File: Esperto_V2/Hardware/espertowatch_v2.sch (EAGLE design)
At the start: 50 parts, among them J1 SM02B, J2 47346-0001, Q1 DMP2035U, U1 AP2112K-3.3V, U2 MCP73832, U3 MAX1921EUT18+T, U4 ATSAMD21G-A, U5 MAX30102EFD+, U6 MAX14595ETAT, U7 MB85RC256VPF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

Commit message: Added new hardware and EAGLE libraries
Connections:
- net 3V3: now also J3.7; no longer J3.2
- net GND: now also J3.4, J3.8; no longer J3.1, J3.5
- net SCL: now also J3.6; no longer J3.3
- net SDA: now also J3.5; no longer J3.4
- net SWCLK: now also J3.2; no longer J3.7
- net SWDIO: now also J3.1; no longer J3.8
- net SWRST: now also J3.3; no longer J3.6
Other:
- moved on the sheet: J3

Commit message: BLE support for APP - bug fixes
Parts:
- C15, C18: value 1uF -> 1.0uF; device CAPACITOR:C-EUC0402_MURATA_GRM15-GJM15 -> CAPACITOR:C-EUC0603_MURATA_GRM18
- C21, C3: device CAPACITOR:C-EUC0201_MURATA_GRM03 -> CAPACITOR:C-EUC0402_MURATA_GRM15-GJM15
- C4, C9: device CAPACITOR:C-EUC0402_MURATA_GRM15-GJM15 -> CAPACITOR:C-EUC0603_MURATA_GRM18
- L1: device INDUCTOR:L-EUL0402_MURATA_LQP15_LQG15 -> INDUCTOR:L-EUL0805_TDK_MLZ
- R1, R4: device RESISTOR:CRCW02011M00FKED -> RESISTOR:CRCW04021M00FKED
- R12, R5: device RESISTOR:CRCW0402100KFKED -> RESISTOR:R-EU_R0603_VISHAY_MCT0603
- R2: device RESISTOR:CRCW0201100KFKED -> RESISTOR:R-EU_R0603_VISHAY_MCT0603
- R7: device RESISTOR:CRCW040210K0FKED -> RESISTOR:R-EU_R0402_VISHAY_CRCW0402
- U3: value MAX1921EUT18+T -> MAX1921EUT18+
- U6: value MAX14595ETAT -> MAX14595ETA+
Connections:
- net GND: now also R5.1; no longer R5.2
- net VUSB: now also R5.2; no longer R5.1
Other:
- moved on the sheet: R5

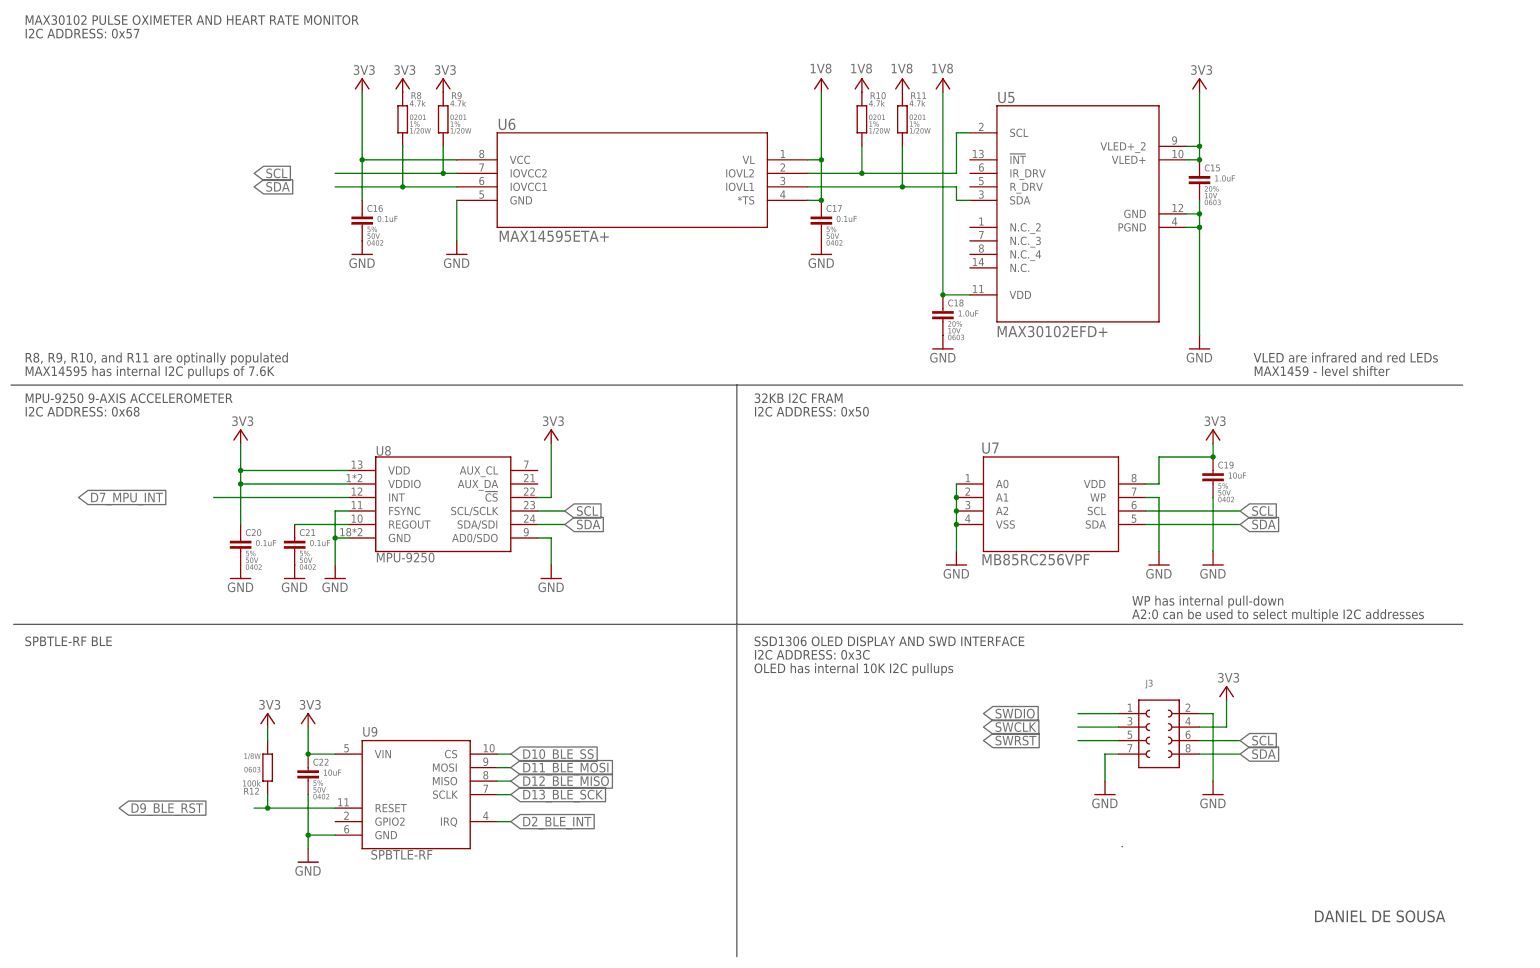
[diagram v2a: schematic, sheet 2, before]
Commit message: Removed I2C pullups
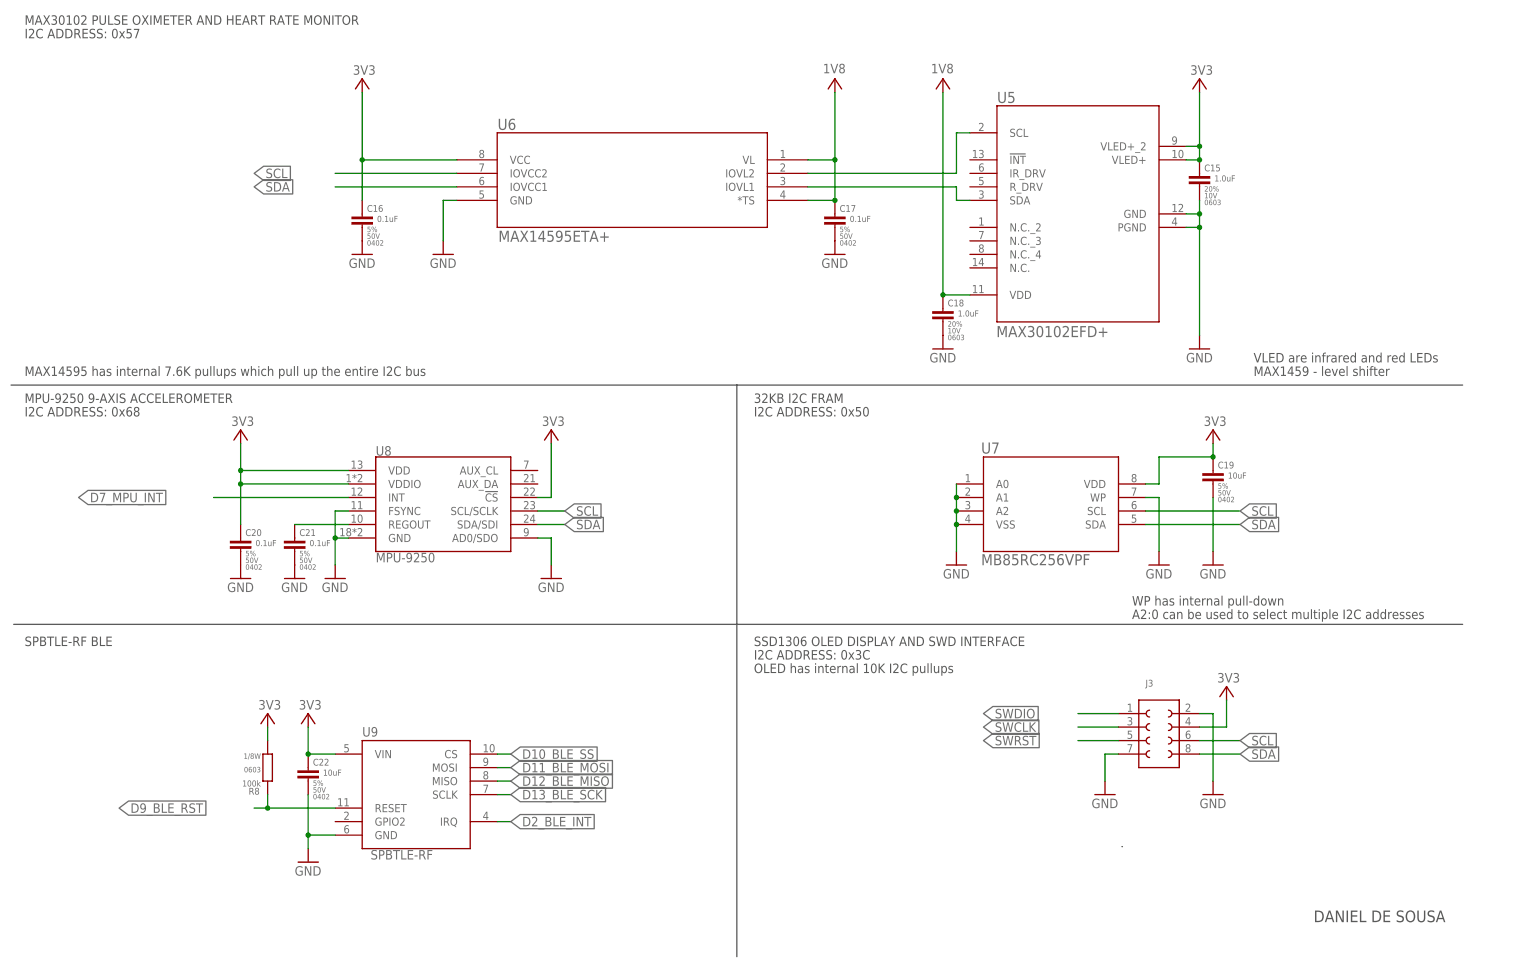
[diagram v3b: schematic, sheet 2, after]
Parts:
- removed R10, R11, R9: 4.7k, RESISTOR:CRCW02014K70FKED
- removed R12: 100k, RESISTOR:R-EU_R0603_VISHAY_MCT0603
- R8: value 4.7k -> 100k; device RESISTOR:CRCW02014K70FKED -> RESISTOR:R-EU_R0603_VISHAY_MCT0603
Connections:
- net 1V8: no longer R10.1, R11.1
- net 3V3: now also R8.2; no longer R12.2, R8.1, R9.1
- net D9_BLE_RST: now also R8.1; no longer R12.1
- net N$16: no longer R10.2
- net N$17: no longer R11.2
- net SCL: no longer R9.2
- net SDA: no longer R8.2
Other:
- note added: "MAX14595 has internal 7.6K pullups which pull up the entire I2C bus"
- note removed: "MAX14595 has internal I2C pullups of 7.6K"
- note removed: "R8, R9, R10, and R11 are optinally populated"
- moved on the sheet: C17, R8
